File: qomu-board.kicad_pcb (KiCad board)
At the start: 6 copper layers, 28.1 x 10.7 mm, 65 parts, among them IC1 EOS-S3, J1 FTSH-105-01-L-DV-K, J2 825437-4, J3 MC-HVT1-S02-G, Q1 RV1C002UN, Q2 RV1C002UN, Q3 RV1C002UN, SW2 Captouch Pads, U1 MIC5504-3.3YMT, U10 UHD1110-FKA, U2 MIC5504-3.3YMT, U4 GD25Q16CEIGR, U5 MC3635, U9 USB-B

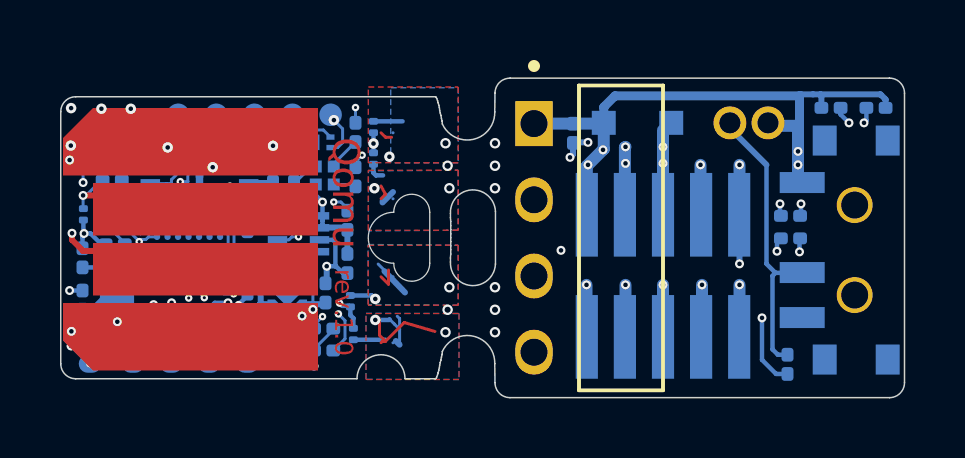
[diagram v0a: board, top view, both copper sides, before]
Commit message: Added logotypes, updated copper ballance
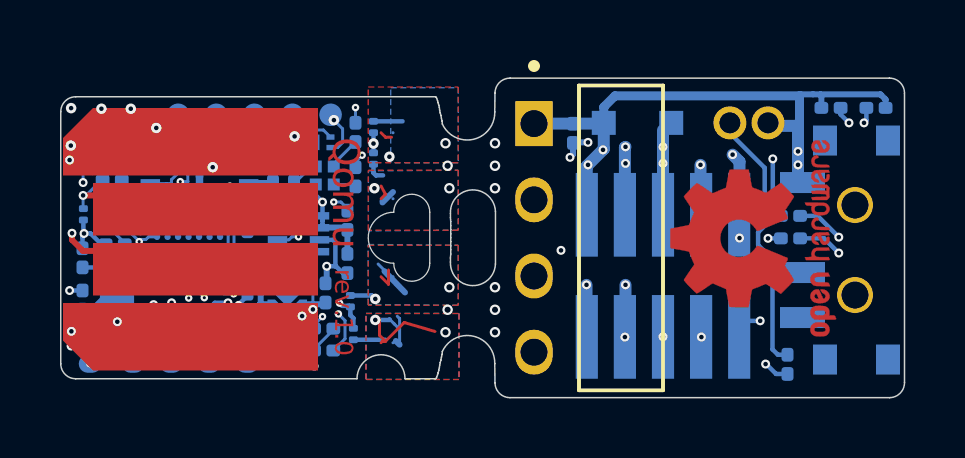
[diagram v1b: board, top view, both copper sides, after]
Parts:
- added N1: oshw_logo, qomu-board-footprints:OSHW-Logo2_7.3x6mm_Copper_Mask, F.Cu at (40.1, 21.8)
- added N2: antmicro_logo, qomu-board-footprints:antmicro-logo_midlayer, F.Cu at (22.4, 20.8)
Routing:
- net /SWD_CLK: track 33.9 -> 31.1 mm, vias 3 -> 4
- net /SWD_IO: track 34.6 -> 31.9 mm
- net /UART_TX: track 23.1 -> 25.1 mm
- net /C1: track 28.7 -> 27.9 mm
- net Net-(J1-Pad8): track 6.56 -> 7.24 mm
- net GND: track 52.8 -> 53.4 mm
- added copper zone on In2.Cu, net GND

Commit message: Updated descriptions on silk overlay
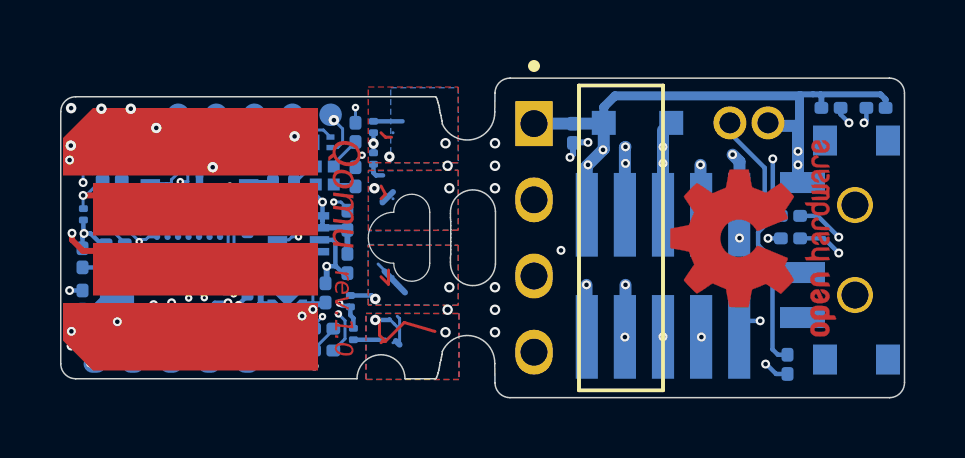
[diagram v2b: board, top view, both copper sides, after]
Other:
- board text added: "+"
- board text added: "1"
- board text added: "C"
- board text added: "E"
- board text added: "F"
- board text added: "GND"
- board text added: "ON"
- board text added: "R"
- board text added: "RX"
- board text added: "TX"

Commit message: Updated signage
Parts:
- added N3: ql_logo, qomu-board-footprints:Ql_logo_mid_9mm, F.Cu at (21.4, 22.3)
- N2: footprint qomu-board-footprints:antmicro-logo_midlayer -> qomu-board-footprints:antmicro-logo_midlayer_4mm
- moved N2 14.7 mm to (37.1, 21.6), turned to 0 degrees
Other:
- board text added: "qomu"
- board text added: "v.1.0"
- board text removed: "Qomu"

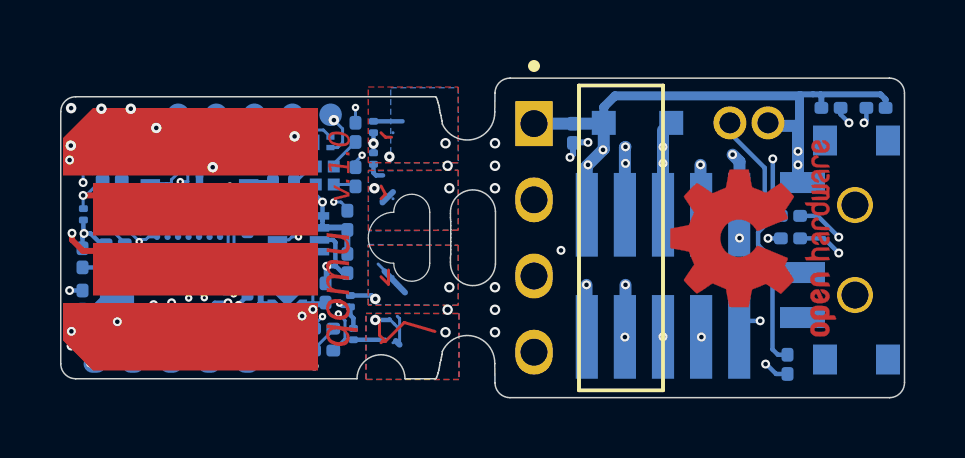
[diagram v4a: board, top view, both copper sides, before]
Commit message: PCB adopted to narrower version of GD25Q16, revision changed to 1.1
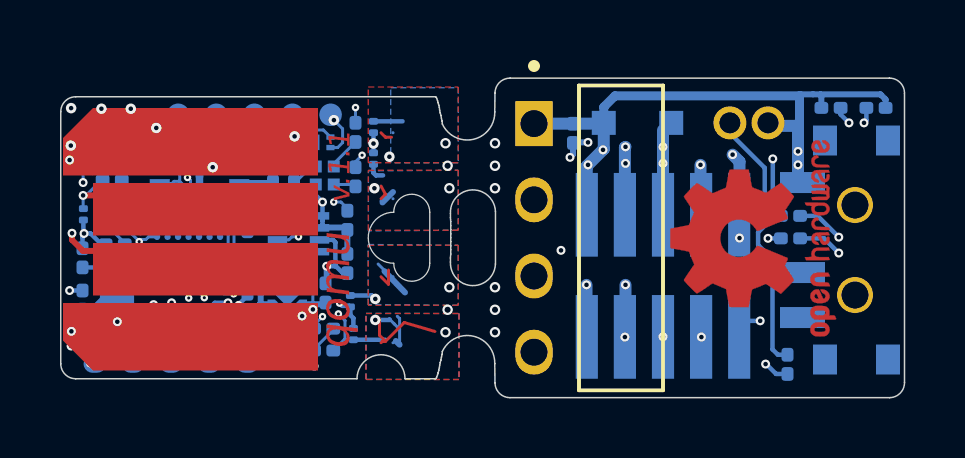
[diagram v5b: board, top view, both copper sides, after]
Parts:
- U4: value GD25Q16CEIGR -> GD25Q16C; footprint qomu-board:GD25Q16CEIGR -> qomu-board-footprints:GD25Q16CEIGR
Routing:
- net GND: track 53.4 -> 51.3 mm
- net +3V3: track 57.9 -> 58.5 mm
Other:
- board text added: "rev.1.1"
- board text added: "v.1.1"
- board text removed: "rev.1.0"
- board text removed: "v.1.0"

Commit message: Updated README
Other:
- board size 28.1 x 10.7 mm -> 28.1 x 10.6 mm
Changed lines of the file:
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@@
-(kicad_pcb (version 20171130) (host pcbnew 5.1.4+dfsg1-1~bpo10+1)
+(kicad_pcb (version 20171130) (host pcbnew 5.1.4-e60b266~84~ubuntu18.04.1)
   (general
     (thickness 0.6)
@@
     (42 Eco1.User user hide)
     (43 Eco2.User user hide)
-    (44 Edge.Cuts user hide)
+    (44 Edge.Cuts user)
     (45 Margin user hide)
     (46 B.CrtYd user hide)
@@
   )
   (gr_arc (start 44.65 26.63) (end 44.65 27.13) (angle -90) (layer Edge.Cuts) (width 0.05))
-  (gr_arc (start 44.65 16.979) (end 45.15 16.979) (angle -90) (layer Edge.Cuts) (width 0.05))
+  (gr_arc (start 44.65 16.98) (end 45.15 16.98) (angle -90) (layer Edge.Cuts) (width 0.05))
   (gr_line (start 31.515 22.68) (end 31.515 20.92) (layer Edge.Cuts) (width 0.05))
   (gr_arc (start 30.576484 25.973761) (end 31.492032 25.994015) (angle -156.5) (layer Edge.Cuts) (width 0.05))
@@
   (gr_line (start 31.5 26.63) (end 31.492032 25.994015) (layer Edge.Cuts) (width 0.05))
   (gr_arc (start 30.765 20.955) (end 31.515 20.92) (angle -180) (layer Edge.Cuts) (width 0.05))
-  (gr_line (start 45.15 26.63) (end 45.15 16.979) (layer Edge.Cuts) (width 0.05))
+  (gr_line (start 45.15 26.63) (end 45.15 16.98) (layer Edge.Cuts) (width 0.05))
   (gr_line (start 32 27.13) (end 44.65 27.13) (layer Edge.Cuts) (width 0.05))
   (gr_line (start 32 16.48) (end 44.65 16.48) (layer Edge.Cuts) (width 0.05))

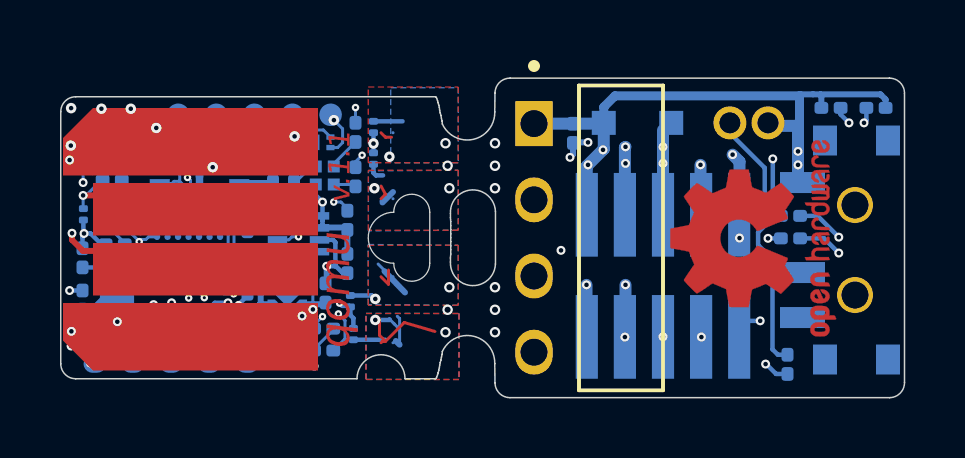
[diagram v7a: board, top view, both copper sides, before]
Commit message: Updated pin 1 marking on RGB LED
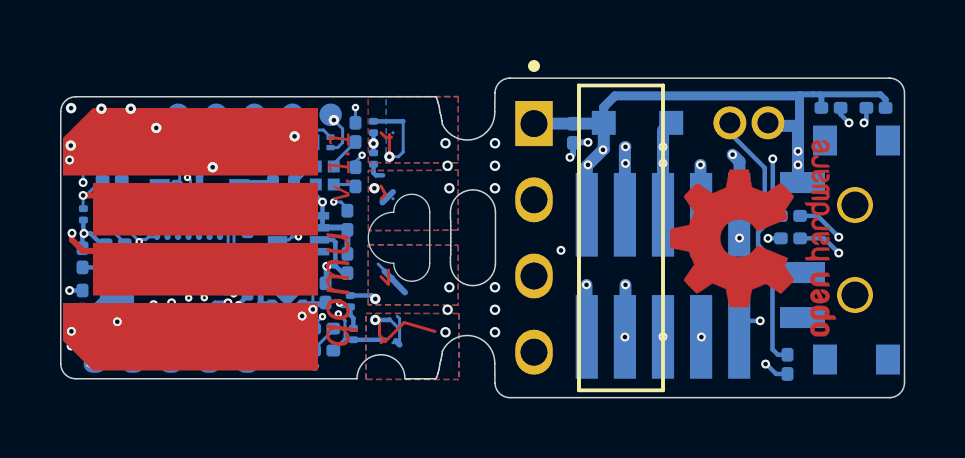
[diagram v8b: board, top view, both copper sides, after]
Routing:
- net /TOUCH_4: track 12.0 -> 14.3 mm
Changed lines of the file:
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@@
-(kicad_pcb (version 20171130) (host pcbnew 5.1.4-e60b266~84~ubuntu18.04.1)
+(kicad_pcb (version 20171130) (host pcbnew 5.1.5-52549c5~84~ubuntu18.04.1)
   (general
     (thickness 0.6)
     (drawings 186)
-    (tracks 1017)
+    (tracks 1022)
     (zones 0)
     (modules 68)
@@
   )
   (layers
-    (0 Top signal hide)
+    (0 Top signal)
     (1 In1.Cu signal hide)
     (2 In2.Cu signal hide)
@@
     (34 B.Paste user hide)
     (35 F.Paste user hide)
-    (36 B.SilkS user hide)
+    (36 B.SilkS user)
     (37 F.SilkS user hide)
     (38 B.Mask user hide)
@@
     (46 B.CrtYd user hide)
     (47 F.CrtYd user hide)
-    (48 B.Fab user hide)
+    (48 B.Fab user)
     (49 F.Fab user hide)
   )
@@
     (add_net "Net-(S1-Pad3)")
   )
+  (module qomu-board-footprints:LED-RGB-5DS-UHD1110-FKA (layer Bottom)
+    (at 25.825 19.725 180)
+    (attr smd)
+    (fp_text reference U10 (at -0.8 -0.2 90) (layer B.SilkS) hide
+      (effects (font (size 0.2 0.2) (thickness 0.05)) (justify mirror))
+    )
+    (fp_text value UHD1110-FKA (at 0.1 0.7) (layer B.Fab) hide
+      (effects (font (size 0.1 0.1) (thickness 0.025)) (justify mirror))
+    )
+    (fp_text user A (at 0.3048 -0.3048) (layer B.Fab)
+      (effects (font (size 0.2 0.2) (thickness 0.05)) (justify mirror))
+    )
+    (fp_line (start 0.525 0.4572) (end 0.4572 0.525) (layer B.Fab) (width 0.05))
+    (fp_line (start -0.525 -0.525) (end -0.525 0.525) (layer B.Fab) (width 0.05))
+    (fp_line (start 0.525 -0.525) (end -0.525 -0.525) (layer B.Fab) (width 0.05))
+    (fp_line (start 0.525 0.4572) (end 0.525 -0.525) (layer B.Fab) (width 0.05))
+    (fp_line (start -0.525 0.525) (end 0.4572 0.525) (layer B.Fab) (width 0.05))
+    (fp_text user %R (at 0 0) (layer B.Fab) hide
+      (effects (font (size 0.25 0.25) (thickness 0.0625)) (justify mirror))
+    )
+    (fp_line (start -0.6 0.6) (end 0.6 0.6) (layer B.CrtYd) (width 0.03))
+    (fp_line (start 0.6 0.6) (end 0.6 -0.6) (layer B.CrtYd) (width 0.03))
+    (fp_line (start 0.6 -0.6) (end -0.6 -0.6) (layer B.CrtYd) (width 0.03))
+    (fp_line (start -0.6 -0.6) (end -0.6 0.6) (layer B.CrtYd) (width 0.03))
+    (fp_circle (center 0.635 0.6604) (end 0.675 0.6604) (layer B.SilkS) (width 0.1))
+    (pad 2 smd rect (at -0.3 0.3 180) (size 0.4 0.4) (layers Bottom B.Paste B.Mask)
+      (net 40 /LED_GK))
+    (pad 1 smd rect (at 0.3 0.3 180) (size 0.4 0.4) (layers Bottom B.Paste B.Mask)
+      (net 39 /LED_BK))
+    (pad 3 smd rect (at -0.3 -0.3 180) (size 0.4 0.4) (layers Bottom B.Paste B.Mask)
+      (net 41 /LED_RK))
+    (pad 4 smd rect (at 0.3 -0.3 180) (size 0.4 0.4) (layers Bottom B.Paste B.Mask)
+      (net 2 +3V3))
+    (model ${KIPRJMOD}/lib/qomu-board-footprints/LED_WS2812B-PLCC4.wrl
+      (offset (xyz 0 0 -0.03))
+      (scale (xyz 0.07000000000000001 0.07000000000000001 0.05))
+      (rotate (xyz 0 0 0))
+    )
+  )
   (module qomu-board-footprints:GD25Q16CEIGR locked (layer Bottom)
     (at 21.65 19.745)
@@
       (effects (font (size 1 1) (thickness 0.15)) (justify mirror))
     )
-    (fp_text value MC3635 (at -0.26 -2.15) (layer B.Fab)
-      (effects (font (size 1 1) (thickness 0.15)) (justify mirror))
+    (fp_text value MC3635 (at -0.29 0) (layer B.Fab) hide
+      (effects (font (size 0.2 0.2) (thickness 0.05)) (justify mirror))
     )
     (fp_circle (center -1.4 1.27) (end -1.33 1.24) (layer B.SilkS) (width 0.15))
@@
     )
   )
-  (module qomu-board-footprints:LED-RGB-5DS-UHD1110-FKA (layer Bottom)
-    (at 25.825 19.725 180)
-    (attr smd)
-    (fp_text reference U10 (at -0.8 -0.2 90) (layer B.SilkS) hide
-      (effects (font (size 0.2 0.2) (thickness 0.05)) (justify mirror))
-    )
-    (fp_text value UHD1110-FKA (at 0.1 0.7) (layer B.Fab) hide
-      (effects (font (size 0.1 0.1) (thickness 0.025)) (justify mirror))
-    )
-    (fp_line (start -0.525 -0.525) (end -0.525 0.525) (layer B.Fab) (width 0.05))
-    (fp_line (start 0.525 -0.525) (end -0.525 -0.525) (layer B.Fab) (width 0.05))
-    (fp_line (start 0.525 0.525) (end 0.525 -0.525) (layer B.Fab) (width 0.05))
-    (fp_line (start -0.525 0.525) (end 0.525 0.525) (layer B.Fab) (width 0.05))
-    (fp_text user %R (at 0 0) (layer B.Fab) hide
-      (effects (font (size 0.25 0.25) (thickness 0.0625)) (justify mirror))
-    )
-    (fp_line (start -0.6 0.6) (end 0.6 0.6) (layer B.CrtYd) (width 0.03))
-    (fp_line (start 0.6 0.6) (end 0.6 -0.6) (layer B.CrtYd) (width 0.03))
-    (fp_line (start 0.6 -0.6) (end -0.6 -0.6) (layer B.CrtYd) (width 0.03))
-    (fp_line (start -0.6 -0.6) (end -0.6 0.6) (layer B.CrtYd) (width 0.03))
-    (fp_circle (center -0.65 0.65) (end -0.614645 0.65) (layer B.SilkS) (width 0.1))
-    (pad 2 smd rect (at -0.3 0.3 180) (size 0.4 0.4) (layers Bottom B.Paste B.Mask)
-      (net 40 /LED_GK))
-    (pad 1 smd rect (at 0.3 0.3 180) (size 0.4 0.4) (layers Bottom B.Paste B.Mask)
-      (net 39 /LED_BK))
-    (pad 3 smd rect (at -0.3 -0.3 180) (size 0.4 0.4) (layers Bottom B.Paste B.Mask)
-      (net 41 /LED_RK))
-    (pad 4 smd rect (at 0.3 -0.3 180) (size 0.4 0.4) (layers Bottom B.Paste B.Mask)
-      (net 2 +3V3))
-    (model ${KIPRJMOD}/lib/qomu-board-footprints/LED_WS2812B-PLCC4.wrl
-      (offset (xyz 0 0 -0.03))
-      (scale (xyz 0.07000000000000001 0.07000000000000001 0.05))
-      (rotate (xyz 0 0 0))
-    )
-  )
   (module qomu-board-footprints:Texas_X2SON-4_1x1mm_P0.65mm (layer Bottom)
     (at 19.77 24.919 180)
@@
   (segment (start 27.85 18.45) (end 27.7 18.3) (width 0.1) (layer Top) (net 4))
   (segment (start 28.05 18.45) (end 27.85 18.45) (width 0.1) (layer Top) (net 4))
-  (segment (start 27.45 17.919) (end 28.419 17.919) (width 0.15) (layer Bottom) (net 4))
   (via micro (at 20.935 22.12) (size 0.25) (drill 0.1) (layers In4.Cu Bottom) (net 4))
   (via micro (at 21 21.27) (size 0.25) (drill 0.1) (layers In4.Cu Bottom) (net 4))
@@
   (segment (start 21.72 19.96) (end 21.72 19.24) (width 0.1) (layer In4.Cu) (net 4))
   (segment (start 21.49 20.19) (end 21.72 19.96) (width 0.1) (layer In4.Cu) (net 4))
+  (segment (start 27.98 19.1) (end 27.98 18.36) (width 0.1) (layer Top) (net 4))
+  (segment (start 27.98 19.1) (end 28.28 19.1) (width 0.1) (layer Bottom) (net 4))
+  (segment (start 28.28 19.1) (end 28.44 18.94) (width 0.1) (layer Bottom) (net 4))
+  (segment (start 27.45 17.919) (end 28.44 17.92) (width 0.15) (layer Bottom) (net 4))
+  (segment (start 28.44 18.94) (end 28.44 17.92) (width 0.1) (layer Bottom) (net 4))
+  (segment (start 28.44 17.92) (end 28.419 17.919) (width 0.15) (layer Bottom) (net 4))
   (segment (start 27.75 25.25) (end 27.7 25.3) (width 0.1) (layer Top) (net 5))
   (segment (start 27.85 25.25) (end 27.75 25.25) (width 0.1) (layer Top) (net 5))
@@
     (polygon
       (pts
-        (xy 30.275 16.8) (xy 30.275 19.3) (xy 28.025 19.3) (xy 28.025 16.8)
+        (xy 30.275 17.09) (xy 30.275 19.3) (xy 27.87 19.305) (xy 27.87 17.095)
       )
     )
@@
     (polygon
       (pts
-        (xy 30.275 16.775) (xy 30.275 19.3) (xy 27.275 19.3) (xy 27.275 16.775)
+        (xy 30.27 17.11) (xy 30.275 19.3) (xy 27.275 19.3) (xy 27.27 17.11)
       )
     )
